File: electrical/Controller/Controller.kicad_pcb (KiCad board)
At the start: 2 copper layers, 30 x 45 mm, 49 parts, among them J1 USB4105-GF-A, J2 UART, J3 SWD, J4 TC2030-NL, J5 I2C, SW1 SYS, U1 USBLC6-2P6, U2 LP5912-3.3DRV, U3 W25Q16JVUXIQ, U4 RP2040, U5 ABPMRRV001PD2A3, Y1 ABM8-272-T3

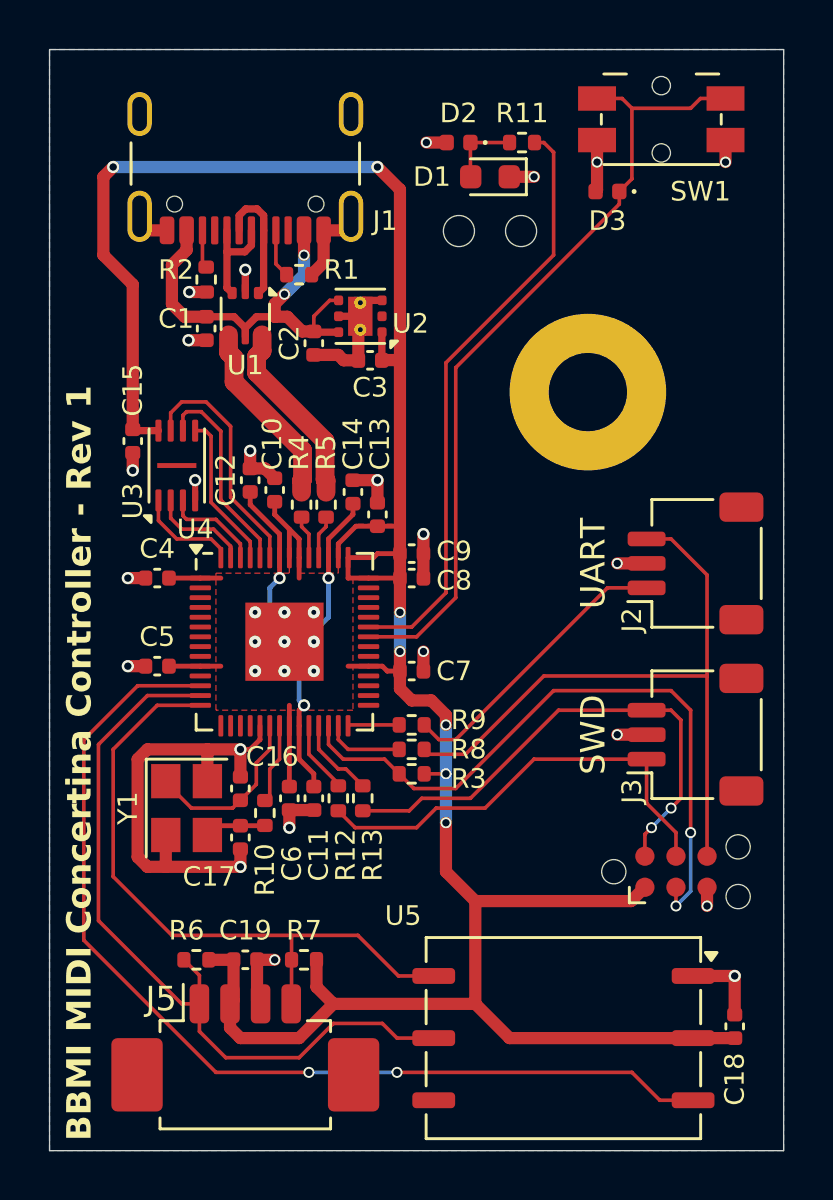
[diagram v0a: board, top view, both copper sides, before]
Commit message: Use 5-pin connector for I2C
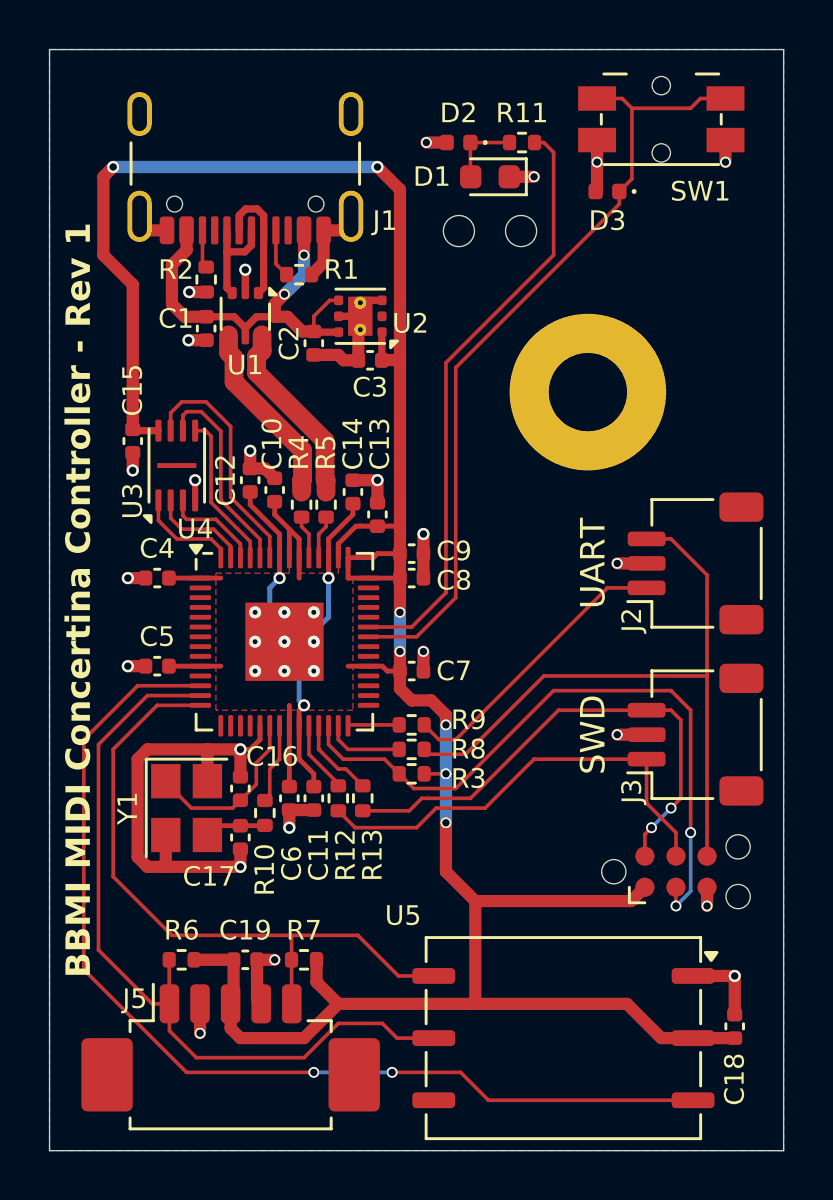
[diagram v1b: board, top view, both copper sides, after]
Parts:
- J5: footprint Connector_Molex:Molex_PicoBlade_53261-0471_1x04-1MP_P1.25mm_Horizontal -> Connector_Molex:Molex_PicoBlade_53261-0571_1x05-1MP_P1.25mm_Horizontal
- moved J5 0.60 mm to (137.4, 111.4)
- moved R6 0.60 mm to (135.4, 107.2)
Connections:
- J5 pad 2: +3.3V -> GND
- J5 pad 3: GND -> +3.3V
- J5 pad 4: I2C_SCL -> GND
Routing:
- net GND: track 56.2 -> 57.4 mm, vias 32 -> 33
- net PRESSURE_INT: track 41.5 -> 42.2 mm
- net +3.3V: track 120.4 -> 121.1 mm

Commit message: More work on controller design
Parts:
- removed the D2 at (146.7, 73.8)
- H2: value SLP-150-150-F -> SLP3-150-150-F
- J2: value UART -> ~
- J3: value SWD -> ~
- J5: value I2C -> ~; footprint Connector_Molex:Molex_PicoBlade_53261-0571_1x05-1MP_P1.25mm_Horizontal -> Connector_Molex:Molex_PicoBlade_53261-0671_1x06-1MP_P1.25mm_Horizontal
- SW1: value SYS -> ~
- Y1: value ABM8-272-T3 -> 12 MHz
- moved R11 19.9 mm to (145.8, 93.4), turned to 0 degrees
- moved J4 1.56 mm to (154.4, 102.6)
- moved C18 1.05 mm to (159.0, 109.6)
- moved U5 1.02 mm to (152.0, 110.2)
- moved H1 1.00 mm to (152.0, 83.0)
- moved J2 1.00 mm to (156.4, 90.0)
- moved J3 1.00 mm to (156.4, 97.0)
- moved J5 0.60 mm to (138.0, 111.4)
- moved D1 0.40 mm to (148.0, 74.8)
- renumbered D3 to D2
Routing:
- net Net-(U4-GPIO25): track 24.5 -> 2.34 mm
- net Net-(D1-A): track 3.01 -> 20.6 mm
- net SWDIO: track 21.0 -> 18.4 mm
- net Net-(D2-K): track 32.8 -> 35.1 mm
- net GND: track 57.4 -> 56.1 mm, vias 33 -> 27
- net I2C_SCL: track 27.1 -> 28.2 mm
- net PRESSURE_INT: track 42.2 -> 43.1 mm
- net UART_RX: track 11.9 -> 12.7 mm
- net I2C_SDA: track 32.2 -> 31.5 mm
- net RUN: track 27.3 -> 27.9 mm
- net SWCLK: track 18.5 -> 19.0 mm
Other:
- outline, holes or cut-outs redrawn
- rule pad_to_mask_clearance: 0.038 -> 0
- board text added: "Enclosure Exterior"
- board text added: "JLCJLCJLCJLC"

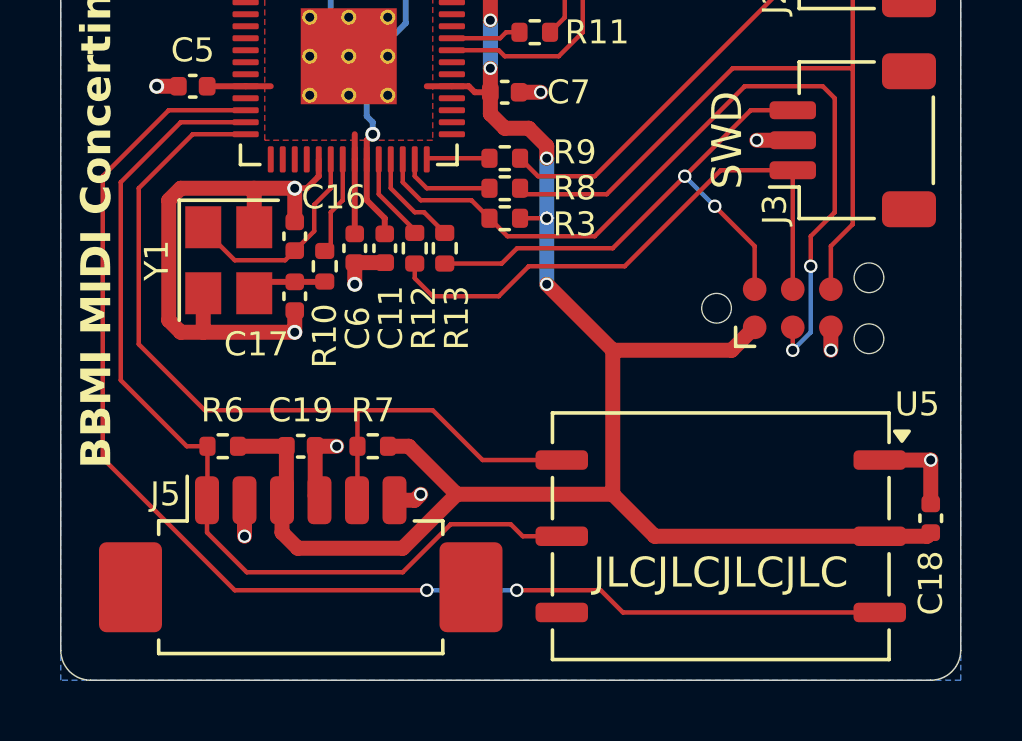
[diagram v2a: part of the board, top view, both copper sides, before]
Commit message: Adjust I2C layout
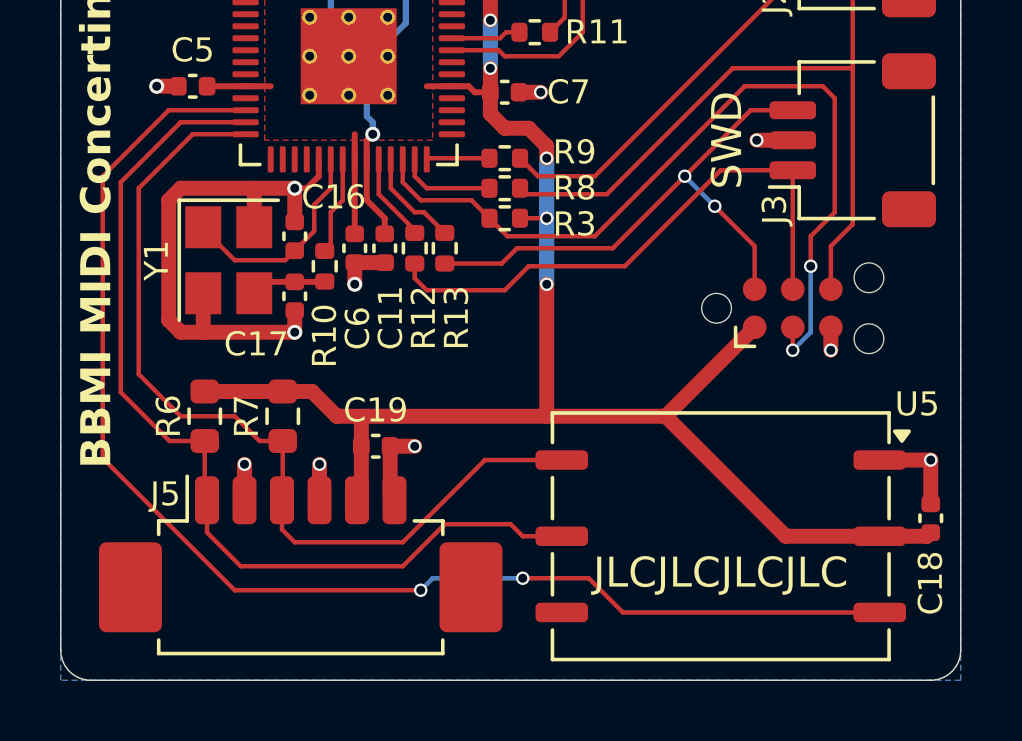
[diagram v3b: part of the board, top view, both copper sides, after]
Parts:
- R6, R7: footprint Resistor_SMD:R_0402_1005Metric -> Resistor_SMD:R_0603_1608Metric
- moved R7 3.16 mm to (137.4, 106.2), turned to -90 degrees
- moved C19 2.50 mm to (140.5, 107.2)
- moved R6 1.17 mm to (134.8, 106.2), turned to -90 degrees
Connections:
- J5 pad 3: +3.3V -> I2C_SCL
- J5 pad 5: I2C_SCL -> +3.3V
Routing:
- net +3.3V: track 121.3 -> 115.4 mm
- net I2C_SCL: track 28.2 -> 29.8 mm

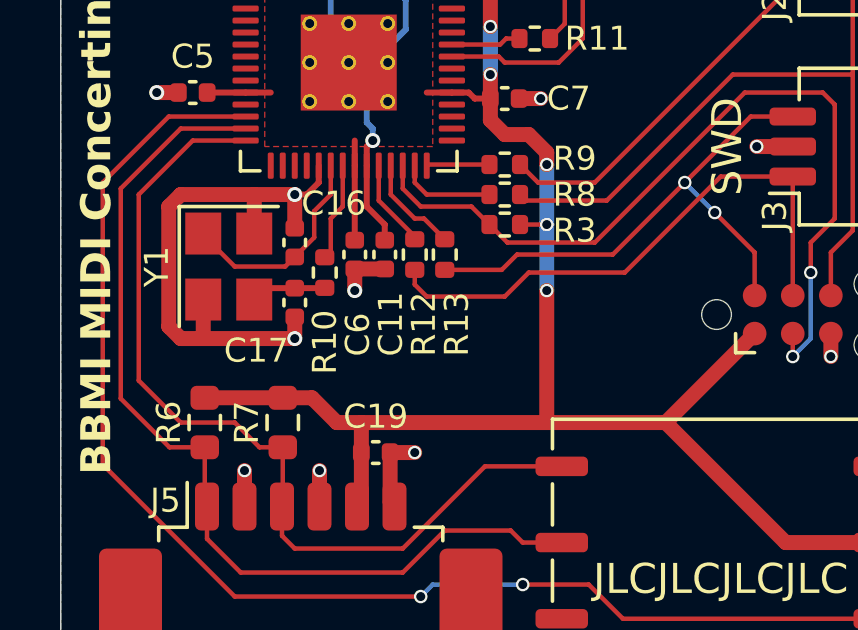
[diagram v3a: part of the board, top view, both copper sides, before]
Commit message: Add Kicad project for right-hand electronics
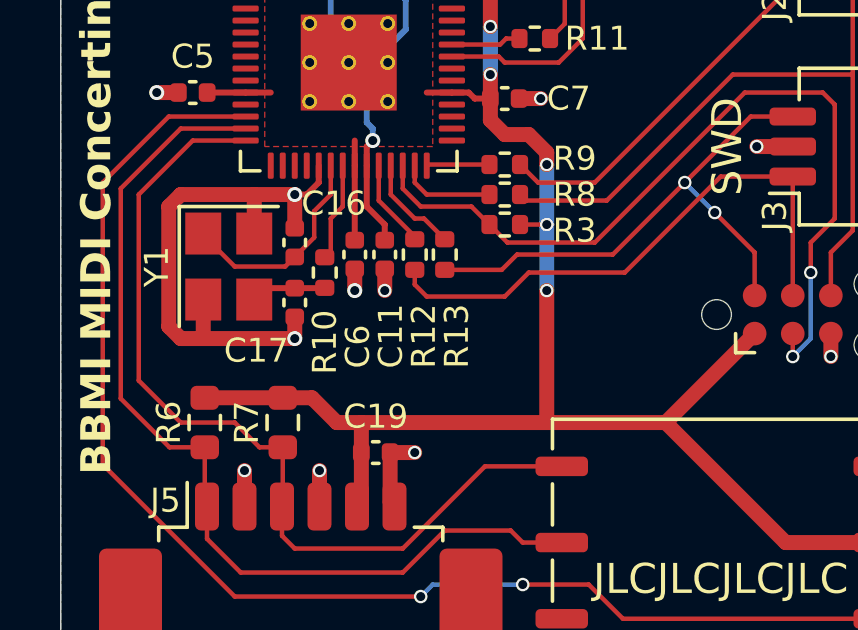
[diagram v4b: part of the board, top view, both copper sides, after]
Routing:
- net GND: track 56.4 -> 56.2 mm, vias 27 -> 28
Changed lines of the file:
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@@
 		)
 	)
+	(footprint "MountingHole:MountingHole_3.2mm_M3_Pad"
+		(layer "F.Cu")
+		(at 152 83)
+		(descr "Mounting Hole 3.2mm, M3")
+		(tags "mounting hole 3.2mm m3")
+		(property "Reference" "H1"
+			(at 0 -4.2 0)
+			(layer "F.SilkS")
+			(hide yes)
+			(effects
+				(font
+					(size 1 1)
+					(thickness 0.15)
+				)
+			)
+		)
+		(property "Value" "MountingHole"
+			(at 0 4.2 0)
+			(layer "F.Fab")
+			(hide yes)
+			(effects
+				(font
+					(size 1 1)
+					(thickness 0.15)
+				)
+			)
+		)
+		(property "Datasheet" ""
+			(at 0 0 0)
+			(unlocked yes)
+			(layer "F.Fab")
+			(hide yes)
+			(effects
+				(font
+					(size 1.27 1.27)
+					(thickness 0.15)
+				)
+			)
+		)
+		(property "Description" "Mounting Hole with connection"
+			(at 0 0 0)
+			(unlocked yes)
+			(layer "F.Fab")
+			(hide yes)
+			(effects
+				(font
+					(size 1.27 1.27)
+					(thickness 0.15)
+				)
+			)
+		)
+		(property "Part" ""
+			(at 0 0 0)
+			(unlocked yes)
+			(layer "F.Fab")
+			(hide yes)
+			(effects
+				(font
+					(size 1 1)
+					(thickness 0.15)
+				)
+			)
+		)
+		(property ki_fp_filters "MountingHole*Pad*")
+		(sheetname "/")
+		(sheetfile "Controller.kicad_sch")
+		(zone_connect 2)
+		(attr exclude_from_pos_files exclude_from_bom)
+		(fp_circle
+			(center 0 0)
+			(end 3.2 0)
+			(stroke
+				(width 0.15)
+				(type solid)
+			)
+			(fill no)
+			(layer "Cmts.User")
+		)
+		(fp_circle
+			(center 0 0)
+			(end 3.45 0)
+			(stroke
+				(width 0.05)
+				(type solid)
+			)
+			(fill no)
+			(layer "F.CrtYd")
+		)
+		(fp_text user "${REFERENCE}"
+			(at 0 0 0)
+			(layer "F.Fab")
+			(effects
+				(font
+					(size 1 1)
+					(thickness 0.15)
+				)
+			)
+		)
+		(pad "1" thru_hole circle
+			(at 0 0)
+			(size 6.4 6.4)
+			(drill 3.2)
+			(layers "*.Cu" "*.Mask")
+			(remove_unused_layers no)
+			(net 2 "GND")
+			(pinfunction "1")
+			(pintype "input")
+		)
+		(embedded_fonts no)
+	)
 	(footprint "Resistor_SMD:R_0402_1005Metric"
 		(layer "F.Cu")
@@
 		(tags "resistor")
 		(property "Reference" "R12"
-			(at 3.4 -0.3 90)
+			(at 3.8 -0.3 90)
 			(layer "F.SilkS")
 			(effects
@@
 		(tags "resistor")
 		(property "Reference" "R13"
-			(at 3.4 -0.4 90)
+			(at 3.8 -0.4 90)
 			(layer "F.SilkS")
 			(effects
@@
 		(tags "capacitor")
 		(property "Reference" "C11"
-			(at 3.4 -0.2 90)
+			(at 3.8 -0.2 90)
 			(layer "F.SilkS")
 			(effects
@@
 		(tags "capacitor")
 		(property "Reference" "C6"
-			(at 3.4 -0.1 90)
+			(at 3.8 -0.1 90)
 			(layer "F.SilkS")
 			(effects
@@
 		)
 	)
-	(footprint "MountingHole:MountingHole_3.2mm_M3_Pad"
-		(layer "F.Cu")
-		(at 152 83)
-		(descr "Mounting Hole 3.2mm, M3")
-		(tags "mounting hole 3.2mm m3")
-		(property "Reference" "H1"
-			(at 0 -4.2 0)
-			(layer "F.SilkS")
-			(hide yes)
-			(effects
-				(font
-					(size 1 1)
-					(thickness 0.15)
-				)
-			)
-		)
-		(property "Value" "MountingHole"
-			(at 0 4.2 0)
-			(layer "F.Fab")
-			(hide yes)
-			(effects
-				(font
-					(size 1 1)
-					(thickness 0.15)
-				)
-			)
-		)
-		(property "Datasheet" ""
-			(at 0 0 0)
-			(unlocked yes)
-			(layer "F.Fab")
-			(hide yes)
-			(effects
-				(font
-					(size 1.27 1.27)
-					(thickness 0.15)
-				)
-			)
-		)
-		(property "Description" "Mounting Hole with connection"
-			(at 0 0 0)
-			(unlocked yes)
-			(layer "F.Fab")
-			(hide yes)
-			(effects
-				(font
-					(size 1.27 1.27)
-					(thickness 0.15)
-				)
-			)
-		)
-		(property "Part" ""
-			(at 0 0 0)
-			(unlocked yes)
-			(layer "F.Fab")
-			(hide yes)
-			(effects
-				(font
-					(size 1 1)
-					(thickness 0.15)
-				)
-			)
-		)
-		(property ki_fp_filters "MountingHole*Pad*")
-		(sheetname "/")
-		(sheetfile "Controller.kicad_sch")
-		(attr exclude_from_pos_files exclude_from_bom)
-		(fp_circle
-			(center 0 0)
-			(end 3.2 0)
-			(stroke
-				(width 0.15)
-				(type solid)
-			)
-			(fill no)
-			(layer "Cmts.User")
-		)
-		(fp_circle
-			(center 0 0)
-			(end 3.45 0)
-			(stroke
-				(width 0.05)
-				(type solid)
-			)
-			(fill no)
-			(layer "F.CrtYd")
-		)
-		(fp_text user "${REFERENCE}"
-			(at 0 0 0)
-			(layer "F.Fab")
-			(effects
-				(font
-					(size 1 1)
-					(thickness 0.15)
-				)
-			)
-		)
-		(pad "1" thru_hole circle
-			(at 0 0)
-			(size 6.4 6.4)
-			(drill 3.2)
-			(layers "*.Cu" "*.Mask")
-			(remove_unused_layers no)
-			(net 2 "GND")
-			(pinfunction "1")
-			(pintype "input")
-			(zone_connect 2)
-		)
-		(embedded_fonts no)
-	)
 	(footprint "Button_Switch_SMD:Panasonic_EVQPUL_EVQPUC"
 		(layer "F.Cu")
@@
 		(layer "User.4")
 		(pts
-			(xy 152 84) (xy 160 70)
+			(xy 152 83) (xy 160 70)
 		)
 		(height -22)
@@
 		)
 		(gr_text "8"
-			(at 156 60.85 0)
+			(at 156 59.85 0)
 			(layer "User.4")
 			(effects
@@
 	)
 	(segment
+		(start 140.8 101.08)
+		(end 140.8 101.8)
+		(width 0.5)
+		(layer "F.Cu")
+		(net 2)
+	)
+	(segment
 		(start 155.67 103.235)
 		(end 155.67 104)
@@
 	)
 	(segment
-		(start 139.8 101.08)
-		(end 140.8 101.08)
-		(width 0.5)
-		(layer "F.Cu")
-		(net 2)
-	)
-	(segment
 		(start 138.625 107.8)
 		(end 138.625 109)
@@
 		(drill 0.3)
 		(layers "F.Cu" "B.Cu")
+		(net 2)
+	)
+	(via
+		(at 140.8 101.8)
+		(size 0.45)
+		(drill 0.3)
+		(layers "F.Cu" "B.Cu")

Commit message: Change board label silkscreen
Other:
- board text added: "MIDI Concertina Controller - Rev 1"
- board text removed: "BBMI MIDI Concertina Controller - Rev 1"
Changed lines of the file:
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@@
 		)
 	)
-	(gr_text "BBMI MIDI Concertina Controller - Rev 1"
+	(gr_text "MIDI Concertina Controller - Rev 1"
 		(at 130.6 92.5 90)
 		(layer "F.SilkS")
